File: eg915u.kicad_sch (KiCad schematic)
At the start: 23 parts, among them J1 SIM_Card, J2 RSP-122811-01, U3 EG915U

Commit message: eg915u: modified page layout, added USB upgrade support (sch + pcb)
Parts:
- added C22: 1uF_10V, Capacitor_SMD:C_0603_1608Metric, symbol Device:C_Small
- added D4: SD05_SOD323, Diode_SMD:D_SOD-323, symbol Diode:SD05_SOD323
- added FL1: DLM0NSN900HY2D, DLM0NSN900HY2D:FIL_DLM0NSN900HY2D, symbol DLM0NSN900HY2D:DLM0NSN900HY2D
- added J4: S4B-ZR-SM4A-TF(LF)(SN), S4B-ZR-SM4A-TF_LF__SN_:JST_S4B-ZR-SM4A-TF(LF)(SN), symbol S4B-ZR-SM4A-TF_LF__SN_:S4B-ZR-SM4A-TF(LF)(SN)
- added JP2: SolderJumper_3_Bridged12, Jumper:SolderJumper-3_P1.3mm_Bridged12_RoundedPad1.0x1.5mm, symbol Jumper:SolderJumper_3_Bridged12
- added R20: 4k7, Resistor_SMD:R_0402_1005Metric, symbol Device:R_Small
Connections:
- net GNDREF: now also C22.1, D4.2 (A2), J4.4, J4.S1 (SHIELD), J4.S2 (SHIELD), JP2.1 (A)
- net VDD_EXT: now also R20.2
- net USB_BOOT: now reaches U3.75 (USB_BOOT)
- net USB_BOOT: now also D4.1 (A1), JP2.2 (C)
- net at U3.10 (USB_DM): now also FL1.3
- net USB_VBUS: now reaches U3.8 (USB_VBUS)
- net USB_VBUS: now also C22.2, J4.1
- net at U3.9 (USB_DP): now also FL1.2
- new net: JP2.3 (B), R20.1
- new net USB_DM: FL1.4, J4.3
- new net USB_DP: FL1.1, J4.2
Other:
- moved on the sheet: AE1, C11, C20, D1, D6, D7, J1, R12, R22, R23, R5, R6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

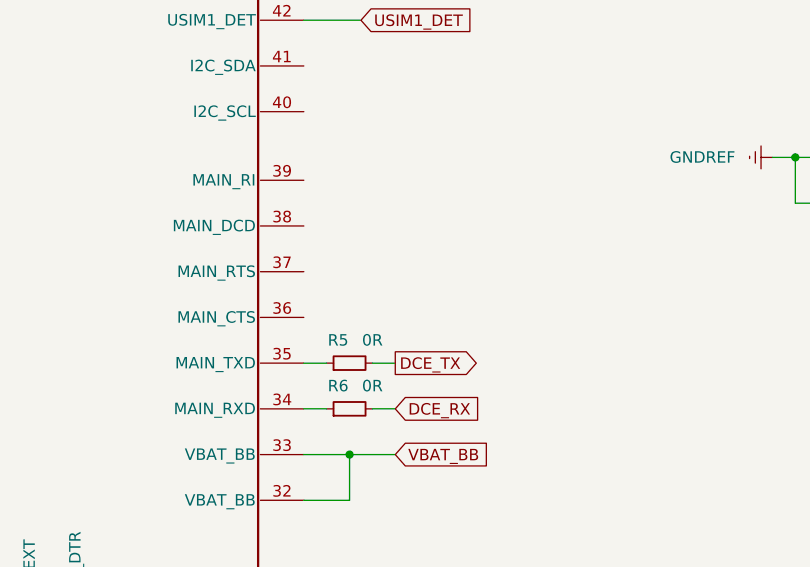
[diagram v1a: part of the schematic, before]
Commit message: added UART flow control pins CTS and RTS
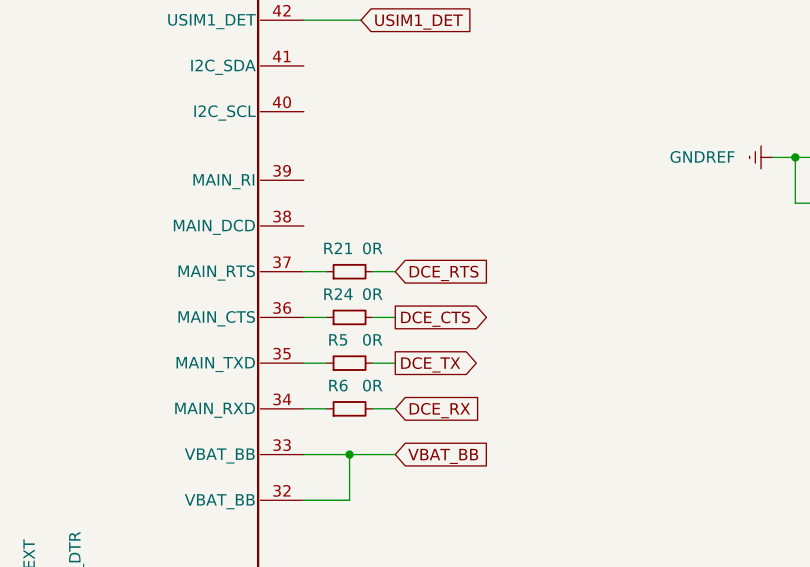
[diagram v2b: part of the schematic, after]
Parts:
- added R21, R24: 0R, Resistor_SMD:R_0402_1005Metric, symbol Device:R_Small
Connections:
- net at U3.36 (MAIN_CTS): now also R24.1
- net at U3.37 (MAIN_RTS): now also R21.1
- new net DCE_CTS: R24.2
- new net DCE_RTS: R21.2
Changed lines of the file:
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@@
+    (stroke (width 0) (type default) (color 0 0 0 0))
+  )
+  (wire (pts (xy 163.83 114.3) (xy 166.37 114.3))
     (stroke (width 0) (type default) (color 0 0 0 0))
   )
@@
     (stroke (width 0) (type default) (color 0 0 0 0))
   )
+  (wire (pts (xy 163.83 119.38) (xy 166.37 119.38))
+    (stroke (width 0) (type default) (color 0 0 0 0))
+  )
   (wire (pts (xy 379.73 181.61) (xy 386.08 181.61))
     (stroke (width 0) (type default) (color 0 0 0 0))
@@
     (stroke (width 0) (type default) (color 0 0 0 0))
   )
+  (wire (pts (xy 156.21 114.3) (xy 158.75 114.3))
+    (stroke (width 0) (type default) (color 0 0 0 0))
+  )
   (wire (pts (xy 156.21 86.36) (xy 162.56 86.36))
     (stroke (width 0) (type default) (color 0 0 0 0))
@@
     (stroke (width 0) (type default) (color 0 0 0 0))
   )
+  (wire (pts (xy 156.21 119.38) (xy 158.75 119.38))
+    (stroke (width 0) (type default) (color 0 0 0 0))
+  )
   (wire (pts (xy 254 53.34) (xy 254 55.88))
     (stroke (width 0) (type default) (color 0 0 0 0))
@@
     )
   )
+  (global_label "DCE_RTS" (shape input) (at 166.37 114.3 0) (fields_autoplaced)
+    (effects (font (size 1.27 1.27)) (justify left))
+    (property "Intersheet References" "${INTERSHEET_REFS}" (id 0) (at 176.8869 114.2206 0)
+      (effects (font (size 1.27 1.27)) (justify left) hide)
+    )
+  )
   (global_label "USIM1_RST" (shape input) (at 267.97 231.14 180) (fields_autoplaced)
     (effects (font (size 1.27 1.27)) (justify right))
@@
     (property "Intersheet References" "${INTERSHEET_REFS}" (id 0) (at 29.8812 124.3806 0)
       (effects (font (size 1.27 1.27)) (justify right) hide)
+    )
+  )
+  (global_label "DCE_CTS" (shape output) (at 166.37 119.38 0) (fields_autoplaced)
+    (effects (font (size 1.27 1.27)) (justify left))
+    (property "Intersheet References" "${INTERSHEET_REFS}" (id 0) (at 176.8869 119.3006 0)
+      (effects (font (size 1.27 1.27)) (justify left) hide)
     )
   )
@@
     (pin "2")
   )
+  (symbol (lib_id "Device:R_Small") (at 161.29 114.3 90) (unit 1)
+    (in_bom yes) (on_board yes)
+    (property "Reference" "R21" (id 0) (at 160.02 111.76 90))
+    (property "Value" "0R" (id 1) (at 163.83 111.76 90))
+    (property "Footprint" "Resistor_SMD:R_0402_1005Metric" (id 2) (at 161.29 114.3 0)
+      (effects (font (size 1.27 1.27)) hide)
+    )
+    (property "Datasheet" "~" (id 3) (at 161.29 114.3 0)
+      (effects (font (size 1.27 1.27)) hide)
+    )
+    (pin "1")
+    (pin "2")
+  )
   (symbol (lib_id "common-mainboard-altium-import:0_EG915U") (at 60.96 238.76 0) (unit 4)
     (in_bom yes) (on_board yes) (fields_autoplaced)
@@
       (effects (font (size 1.27 1.27)) hide)
     )
+    (pin "1")
+    (pin "2")
+  )
+  (symbol (lib_id "Device:R_Small") (at 161.29 119.38 90) (unit 1)
+    (in_bom yes) (on_board yes)
+    (property "Reference" "R24" (id 0) (at 160.02 116.84 90))
+    (property "Value" "0R" (id 1) (at 163.83 116.84 90))
+    (property "Footprint" "Resistor_SMD:R_0402_1005Metric" (id 2) (at 161.29 119.38 0)
+      (effects (font (size 1.27 1.27)) hide)
+    )
+    (property "Datasheet" "~" (id 3) (at 161.29 119.38 0)
+      (effects (font (size 1.27 1.27)) hide)
+    )

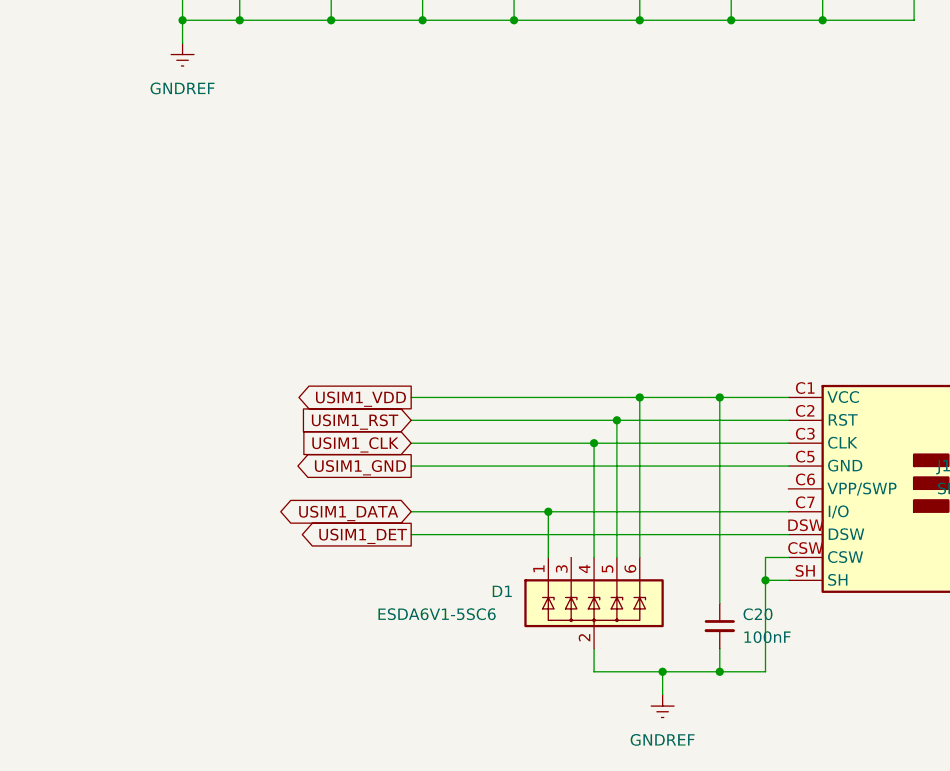
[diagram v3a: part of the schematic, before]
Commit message: sim card: added RF filtering passive components
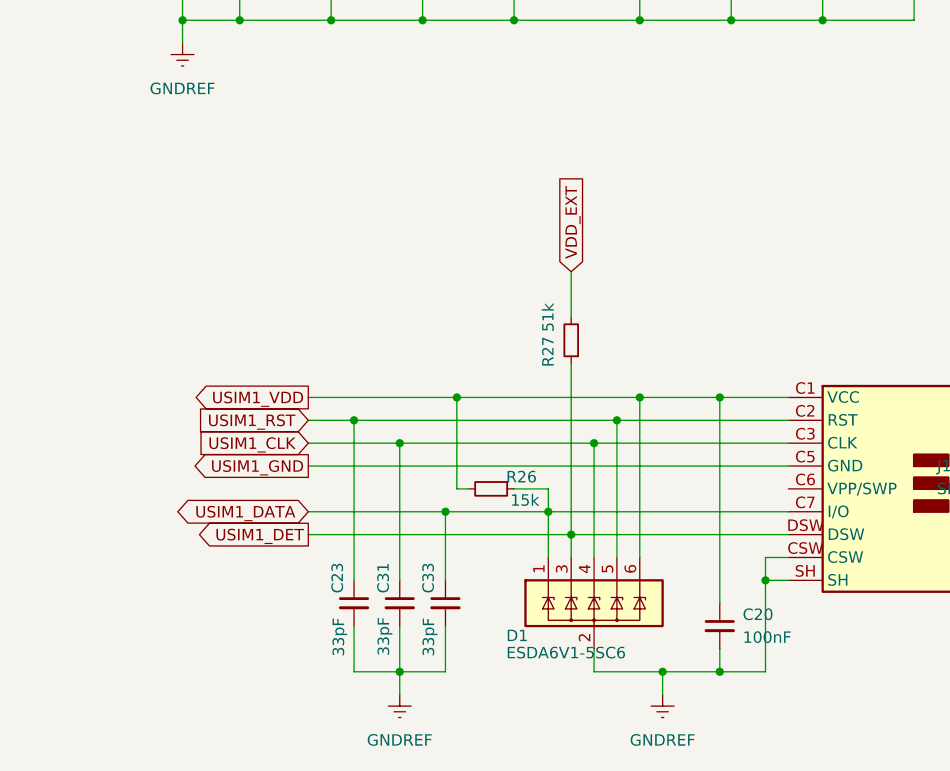
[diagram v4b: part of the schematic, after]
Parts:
- added C23, C31, C33: 33pF, Capacitor_SMD:C_0402_1005Metric, symbol Device:C_Small
- added R26: 15k, Resistor_SMD:R_0402_1005Metric, symbol Device:R_Small
- added R27: 51k, Resistor_SMD:R_0402_1005Metric, symbol Device:R_Small
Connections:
- net GNDREF: now also C23.2, C31.2, C33.2
- net USIM1_CLK: now also C31.1
- net USIM1_DATA: now also C33.1, R26.1
- net USIM1_DET: now also D1.3 (IO2), R27.1
- net USIM1_RST: now also C23.1
- net USIM1_VDD: now also R26.2
- net VDD_EXT: now also R27.2

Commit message: ok before switching to EG91EX footprint
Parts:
- C12, C16: footprint Capacitor_SMD:C_0603_1608Metric -> Capacitor_Tantalum_SMD:CP_EIA-6032-15_Kemet-U
- D2, D4: footprint Diode_SMD:D_SOD-323 -> Diode_SMD:D_SOD-323_HandSoldering
- U3: footprint quectel-lib:_AD LIB_EG915U.PcbLib_EG915U -> EG91EXGA-128-SGNS:XCVR_EG91EXGA-128-SGNS
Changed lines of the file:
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@@
       (effects (font (size 1.27 1.27)) (justify left))
     )
-    (property "Footprint" "Capacitor_SMD:C_0603_1608Metric" (id 2) (at 293.37 177.8 0)
+    (property "Footprint" "Capacitor_Tantalum_SMD:CP_EIA-6032-15_Kemet-U" (id 2) (at 293.37 177.8 0)
       (effects (font (size 1.27 1.27)) hide)
     )
@@
       (effects (font (size 1.27 1.27)) (justify left))
     )
-    (property "Footprint" "quectel-lib:_AD LIB_EG915U.PcbLib_EG915U" (id 2) (at 251.46 93.98 0)
+    (property "Footprint" "EG91EXGA-128-SGNS:XCVR_EG91EXGA-128-SGNS" (id 2) (at 251.46 93.98 0)
       (effects (font (size 1.27 1.27)) hide)
     )
@@
     (property "Reference" "U3" (id 0) (at 60.96 218.44 0))
     (property "Value" "EG915U" (id 1) (at 60.96 220.98 0))
-    (property "Footprint" "quectel-lib:_AD LIB_EG915U.PcbLib_EG915U" (id 2) (at 60.96 238.76 0)
+    (property "Footprint" "EG91EXGA-128-SGNS:XCVR_EG91EXGA-128-SGNS" (id 2) (at 60.96 238.76 0)
       (effects (font (size 1.27 1.27)) hide)
     )
@@
       (effects (font (size 1.27 1.27)) (justify left))
     )
-    (property "Footprint" "quectel-lib:_AD LIB_EG915U.PcbLib_EG915U" (id 2) (at 378.46 95.25 0)
+    (property "Footprint" "EG91EXGA-128-SGNS:XCVR_EG91EXGA-128-SGNS" (id 2) (at 378.46 95.25 0)
       (effects (font (size 1.27 1.27)) hide)
     )
@@
       (effects (font (size 1.27 1.27)) (justify left))
     )
-    (property "Footprint" "quectel-lib:_AD LIB_EG915U.PcbLib_EG915U" (id 2) (at 102.87 93.98 0)
+    (property "Footprint" "EG91EXGA-128-SGNS:XCVR_EG91EXGA-128-SGNS" (id 2) (at 102.87 93.98 0)
       (effects (font (size 1.27 1.27)) hide)
     )
@@
       (effects (font (size 1.27 1.27)) (justify left))
     )
-    (property "Footprint" "Diode_SMD:D_SOD-323" (id 2) (at 194.31 184.15 0)
+    (property "Footprint" "Diode_SMD:D_SOD-323_HandSoldering" (id 2) (at 194.31 184.15 0)
       (effects (font (size 1.27 1.27)) hide)
     )
@@
       (effects (font (size 1.27 1.27)) (justify left))
     )
-    (property "Footprint" "Diode_SMD:D_SOD-323" (id 2) (at 242.57 177.8 90)
+    (property "Footprint" "Diode_SMD:D_SOD-323_HandSoldering" (id 2) (at 242.57 177.8 90)
       (effects (font (size 1.27 1.27)) hide)
     )
@@
       (effects (font (size 1.27 1.27)) (justify left))
     )
-    (property "Footprint" "Capacitor_SMD:C_0603_1608Metric" (id 2) (at 248.92 177.8 0)
-      (effects (font (size 1.27 1.27)) hide)
-    )
+    (property "Footprint" "Capacitor_Tantalum_SMD:CP_EIA-6032-15_Kemet-U" (id 2) (at 248.92 177.8 0)
+      (effects (font (size 1.27 1.27)) hide)
+    )

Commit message: Added 4G modem UART test points
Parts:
- added TP6: DCE_TX, TestPoint:TestPoint_Pad_D1.5mm, symbol Connector:TestPoint
- added TP7: DCE_RX, TestPoint:TestPoint_Pad_D1.5mm, symbol Connector:TestPoint
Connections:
- net DCE_RX: now also TP7.1
- net DCE_TX: now also TP6.1
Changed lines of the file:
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@@
+    (stroke (width 0) (type default) (color 0 0 0 0))
+  )
+  (wire (pts (xy 388.62 214.63) (xy 388.62 219.71))
     (stroke (width 0) (type default) (color 0 0 0 0))
   )
@@
     (stroke (width 0) (type default) (color 0 0 0 0))
   )
+  (wire (pts (xy 393.7 214.63) (xy 393.7 219.71))
+    (stroke (width 0) (type default) (color 0 0 0 0))
+  )
   (wire (pts (xy 156.21 86.36) (xy 162.56 86.36))
     (stroke (width 0) (type default) (color 0 0 0 0))
@@
     )
   )
+  (global_label "DCE_TX" (shape input) (at 388.62 219.71 270) (fields_autoplaced)
+    (effects (font (size 1.27 1.27)) (justify right))
+    (property "Intersheet References" "${INTERSHEET_REFS}" (id 0) (at 388.5406 228.9569 90)
+      (effects (font (size 1.27 1.27)) (justify right) hide)
+    )
+  )
   (global_label "USIM1_GND" (shape output) (at 256.54 236.22 180) (fields_autoplaced)
     (effects (font (size 1.27 1.27)) (justify right))
@@
     (property "Intersheet References" "${INTERSHEET_REFS}" (id 0) (at 340.3541 167.5606 0)
       (effects (font (size 1.27 1.27)) (justify left) hide)
+    )
+  )
+  (global_label "DCE_RX" (shape input) (at 393.7 219.71 270) (fields_autoplaced)
+    (effects (font (size 1.27 1.27)) (justify right))
+    (property "Intersheet References" "${INTERSHEET_REFS}" (id 0) (at 393.7794 229.2593 90)
+      (effects (font (size 1.27 1.27)) (justify right) hide)
     )
   )
@@
     (pin "1")
     (pin "2")
+  )
+  (symbol (lib_id "Connector:TestPoint") (at 393.7 214.63 0) (unit 1)
+    (in_bom yes) (on_board yes)
+    (property "Reference" "TP7" (id 0) (at 392.2345 206.2678 90)
+      (effects (font (size 1.27 1.27)) (justify right))
+    )
+    (property "Value" "DCE_RX" (id 1) (at 394.442 201.6687 90)
+      (effects (font (size 1.27 1.27)) (justify right))
+    )
+    (property "Footprint" "TestPoint:TestPoint_Pad_D1.5mm" (id 2) (at 398.78 214.63 0)
+      (effects (font (size 1.27 1.27)) hide)
+    )
+    (property "Datasheet" "~" (id 3) (at 398.78 214.63 0)
+      (effects (font (size 1.27 1.27)) hide)
+    )
+    (pin "1")
   )
   (symbol (lib_id "Jumper:SolderJumper_3_Bridged12") (at 193.04 177.8 90) (unit 1)
@@
     (pin "G2")
   )
+  (symbol (lib_id "Connector:TestPoint") (at 388.62 214.63 0) (unit 1)
+    (in_bom yes) (on_board yes)
+    (property "Reference" "TP6" (id 0) (at 387.1545 206.2678 90)
+      (effects (font (size 1.27 1.27)) (justify right))
+    )
+    (property "Value" "DCE_TX" (id 1) (at 389.362 201.6687 90)
+      (effects (font (size 1.27 1.27)) (justify right))
+    )
+    (property "Footprint" "TestPoint:TestPoint_Pad_D1.5mm" (id 2) (at 393.7 214.63 0)
+      (effects (font (size 1.27 1.27)) hide)
+    )
+    (property "Datasheet" "~" (id 3) (at 393.7 214.63 0)
+      (effects (font (size 1.27 1.27)) hide)
+    )
+    (pin "1")
+  )
   (symbol (lib_id "power:GNDREF") (at 132.08 255.27 0) (unit 1)
